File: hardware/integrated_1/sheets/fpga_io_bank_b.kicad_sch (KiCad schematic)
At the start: 1 part, among them U1 XC6SLX9-TQG144

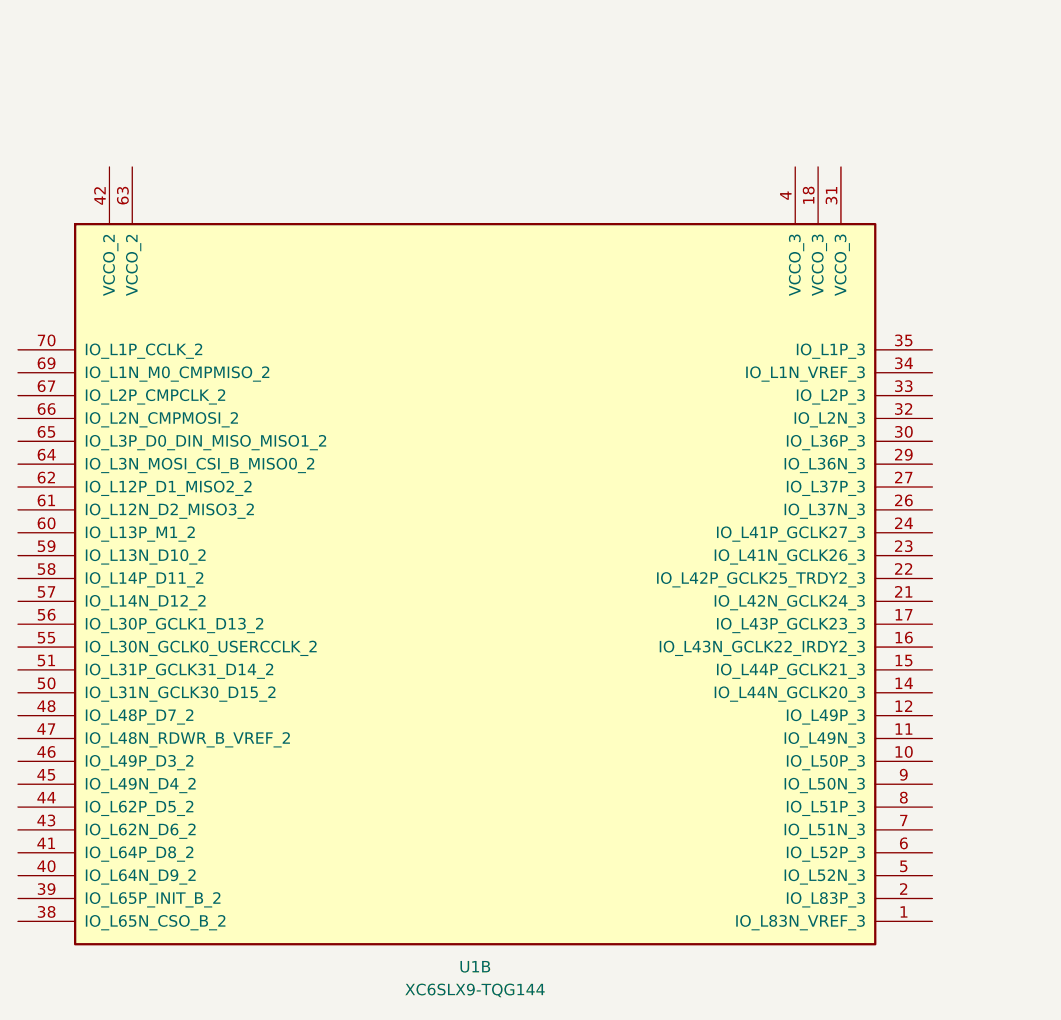
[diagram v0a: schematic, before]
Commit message: hooked up display to fpga
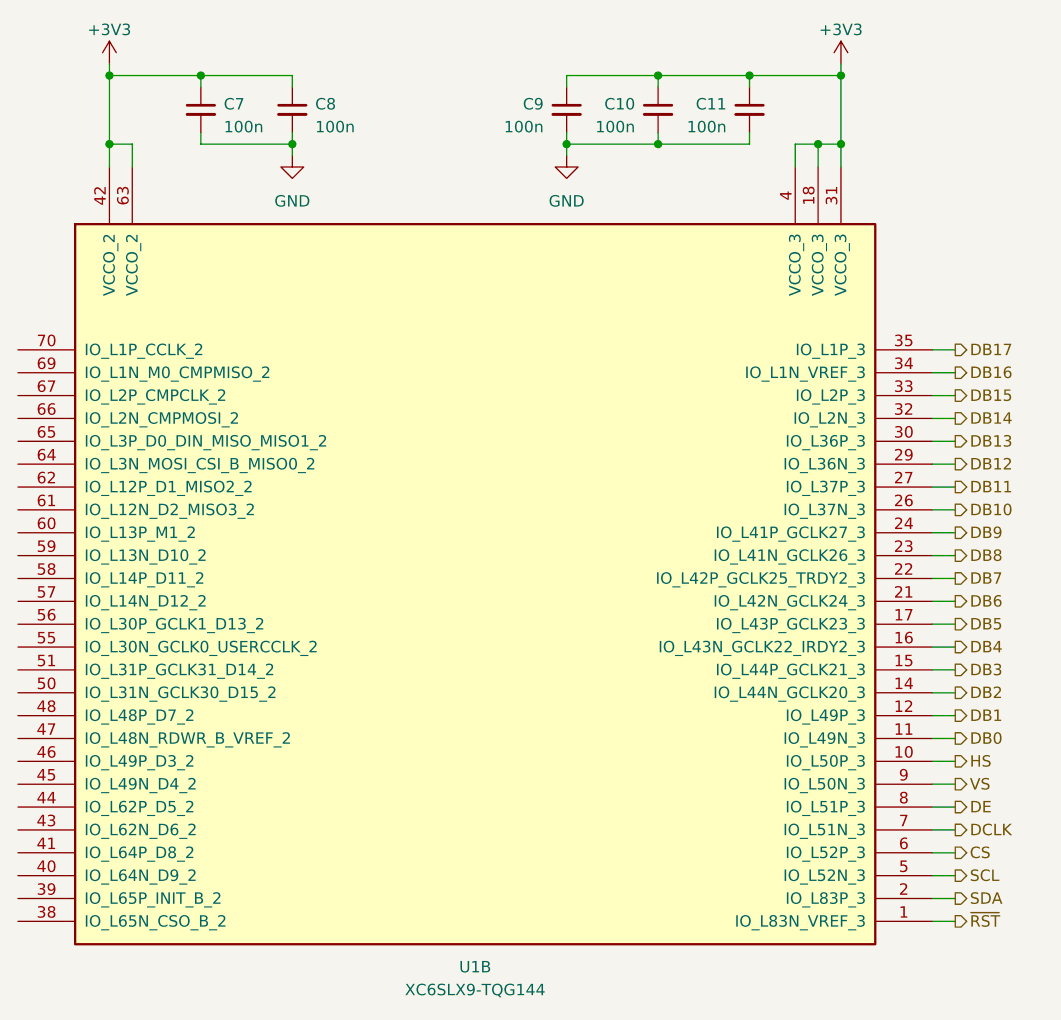
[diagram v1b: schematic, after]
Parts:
- added C10, C11, C7, C8, C9: 100n, Capacitor_SMD:C_0402_1005Metric, symbol Device:C_Small
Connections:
- net ~{RST}: now reaches U1.1 (IO_L83N_VREF_3)
- net HS: now reaches U1.10 (IO_L50P_3)
- net DB0: now reaches U1.11 (IO_L49N_3)
- net DB1: now reaches U1.12 (IO_L49P_3)
- net DB2: now reaches U1.14 (IO_L44N_GCLK20_3)
- net DB3: now reaches U1.15 (IO_L44P_GCLK21_3)
- net DB4: now reaches U1.16 (IO_L43N_GCLK22_IRDY2_3)
- net DB5: now reaches U1.17 (IO_L43P_GCLK23_3)
- net +3V3: now reaches U1.18 (VCCO_3)
- net +3V3: now also U1.31 (VCCO_3), U1.4 (VCCO_3), U1.42 (VCCO_2), U1.63 (VCCO_2), C10.1, C11.1, C7.1, C8.1, C9.1
- net SDA: now reaches U1.2 (IO_L83P_3)
- net DB6: now reaches U1.21 (IO_L42N_GCLK24_3)
- net DB7: now reaches U1.22 (IO_L42P_GCLK25_TRDY2_3)
- net DB8: now reaches U1.23 (IO_L41N_GCLK26_3)
- net DB9: now reaches U1.24 (IO_L41P_GCLK27_3)
- net DB10: now reaches U1.26 (IO_L37N_3)
- net DB11: now reaches U1.27 (IO_L37P_3)
- net DB12: now reaches U1.29 (IO_L36N_3)
- net DB13: now reaches U1.30 (IO_L36P_3)
- net DB14: now reaches U1.32 (IO_L2N_3)
- net DB15: now reaches U1.33 (IO_L2P_3)
- net DB16: now reaches U1.34 (IO_L1N_VREF_3)
- net DB17: now reaches U1.35 (IO_L1P_3)
- net SCL: now reaches U1.5 (IO_L52N_3)
- net CS: now reaches U1.6 (IO_L52P_3)
- net DCLK: now reaches U1.7 (IO_L51N_3)
- net DE: now reaches U1.8 (IO_L51P_3)
- net VS: now reaches U1.9 (IO_L50N_3)
- new net GND: C10.2, C11.2, C7.2, C8.2, C9.2

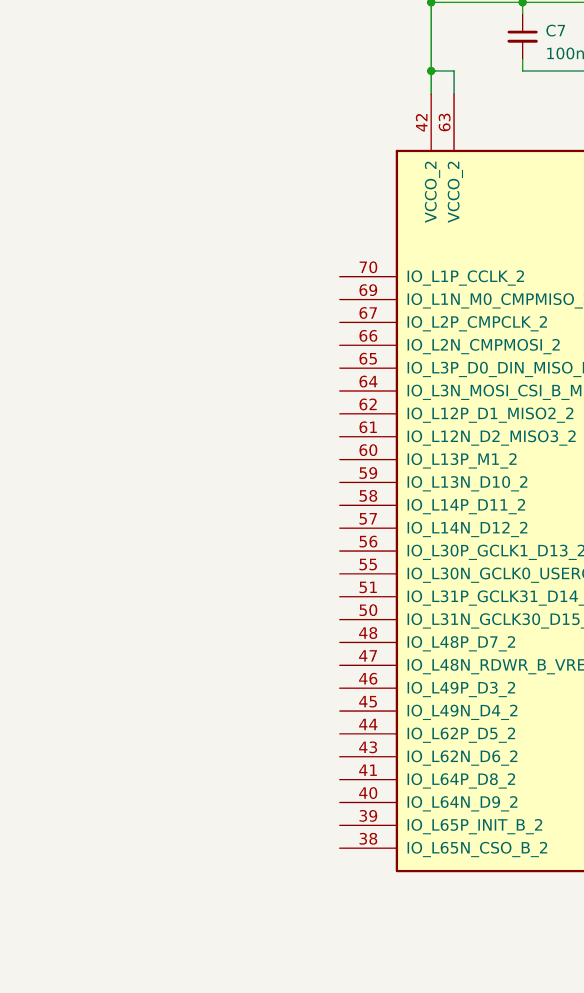
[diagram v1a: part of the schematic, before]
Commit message: rearranged the pinout to make more sense
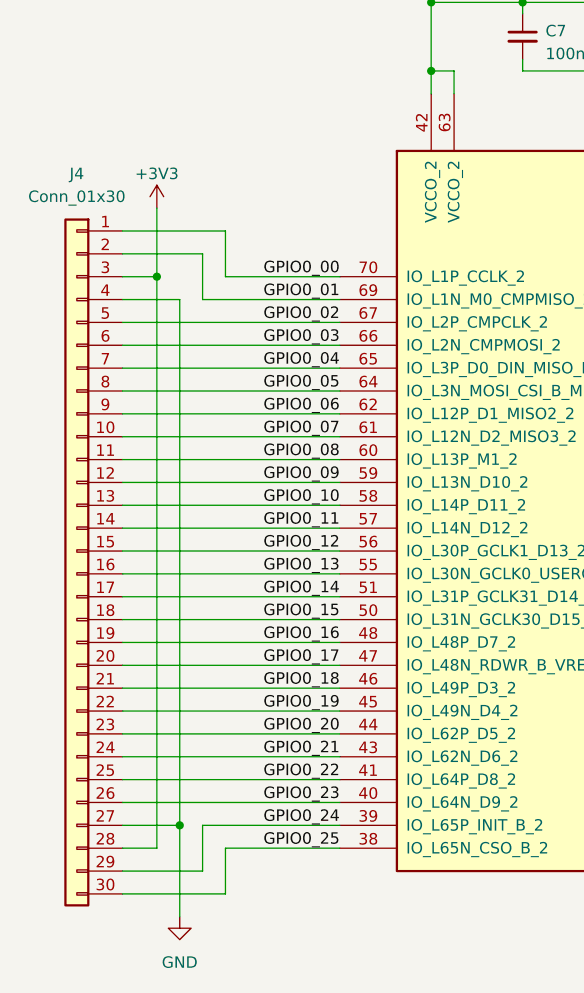
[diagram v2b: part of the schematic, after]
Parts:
- added J4: Conn_01x30, Connector_PinSocket_2.54mm:PinSocket_1x30_P2.54mm_Vertical, symbol Connector_Generic:Conn_01x30
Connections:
- net +3V3: now also J4.28 (Pin_28), J4.3 (Pin_3)
- net GND: now also J4.27 (Pin_27), J4.4 (Pin_4)
- net GPIO0_25: now reaches U1.38 (IO_L65N_CSO_B_2)
- net GPIO0_25: now also J4.30 (Pin_30)
- net GPIO0_24: now reaches U1.39 (IO_L65P_INIT_B_2)
- net GPIO0_24: now also J4.29 (Pin_29)
- net GPIO0_23: now reaches U1.40 (IO_L64N_D9_2)
- net GPIO0_23: now also J4.26 (Pin_26)
- net GPIO0_22: now reaches U1.41 (IO_L64P_D8_2)
- net GPIO0_22: now also J4.25 (Pin_25)
- net GPIO0_21: now reaches U1.43 (IO_L62N_D6_2)
- net GPIO0_21: now also J4.24 (Pin_24)
- net GPIO0_20: now reaches U1.44 (IO_L62P_D5_2)
- net GPIO0_20: now also J4.23 (Pin_23)
- net GPIO0_19: now reaches U1.45 (IO_L49N_D4_2)
- net GPIO0_19: now also J4.22 (Pin_22)
- net GPIO0_18: now reaches U1.46 (IO_L49P_D3_2)
- net GPIO0_18: now also J4.21 (Pin_21)
- net GPIO0_17: now reaches U1.47 (IO_L48N_RDWR_B_VREF_2)
- net GPIO0_17: now also J4.20 (Pin_20)
- net GPIO0_16: now reaches U1.48 (IO_L48P_D7_2)
- net GPIO0_16: now also J4.19 (Pin_19)
- net GPIO0_15: now reaches U1.50 (IO_L31N_GCLK30_D15_2)
- net GPIO0_15: now also J4.18 (Pin_18)
- net GPIO0_14: now reaches U1.51 (IO_L31P_GCLK31_D14_2)
- net GPIO0_14: now also J4.17 (Pin_17)
- net GPIO0_13: now reaches U1.55 (IO_L30N_GCLK0_USERCCLK_2)
- net GPIO0_13: now also J4.16 (Pin_16)
- net GPIO0_12: now reaches U1.56 (IO_L30P_GCLK1_D13_2)
- net GPIO0_12: now also J4.15 (Pin_15)
- net GPIO0_11: now reaches U1.57 (IO_L14N_D12_2)
- net GPIO0_11: now also J4.14 (Pin_14)
- net GPIO0_10: now reaches U1.58 (IO_L14P_D11_2)
- net GPIO0_10: now also J4.13 (Pin_13)
- net GPIO0_09: now reaches U1.59 (IO_L13N_D10_2)
- net GPIO0_09: now also J4.12 (Pin_12)
- net GPIO0_08: now reaches U1.60 (IO_L13P_M1_2)
- net GPIO0_08: now also J4.11 (Pin_11)
- net GPIO0_07: now reaches U1.61 (IO_L12N_D2_MISO3_2)
- net GPIO0_07: now also J4.10 (Pin_10)
- net GPIO0_06: now reaches U1.62 (IO_L12P_D1_MISO2_2)
- net GPIO0_06: now also J4.9 (Pin_9)
- net GPIO0_05: now reaches U1.64 (IO_L3N_MOSI_CSI_B_MISO0_2)
- net GPIO0_05: now also J4.8 (Pin_8)
- net GPIO0_04: now reaches U1.65 (IO_L3P_D0_DIN_MISO_MISO1_2)
- net GPIO0_04: now also J4.7 (Pin_7)
- net GPIO0_03: now reaches U1.66 (IO_L2N_CMPMOSI_2)
- net GPIO0_03: now also J4.6 (Pin_6)
- net GPIO0_02: now reaches U1.67 (IO_L2P_CMPCLK_2)
- net GPIO0_02: now also J4.5 (Pin_5)
- net GPIO0_01: now reaches U1.69 (IO_L1N_M0_CMPMISO_2)
- net GPIO0_01: now also J4.2 (Pin_2)
- net GPIO0_00: now reaches U1.70 (IO_L1P_CCLK_2)
- net GPIO0_00: now also J4.1 (Pin_1)

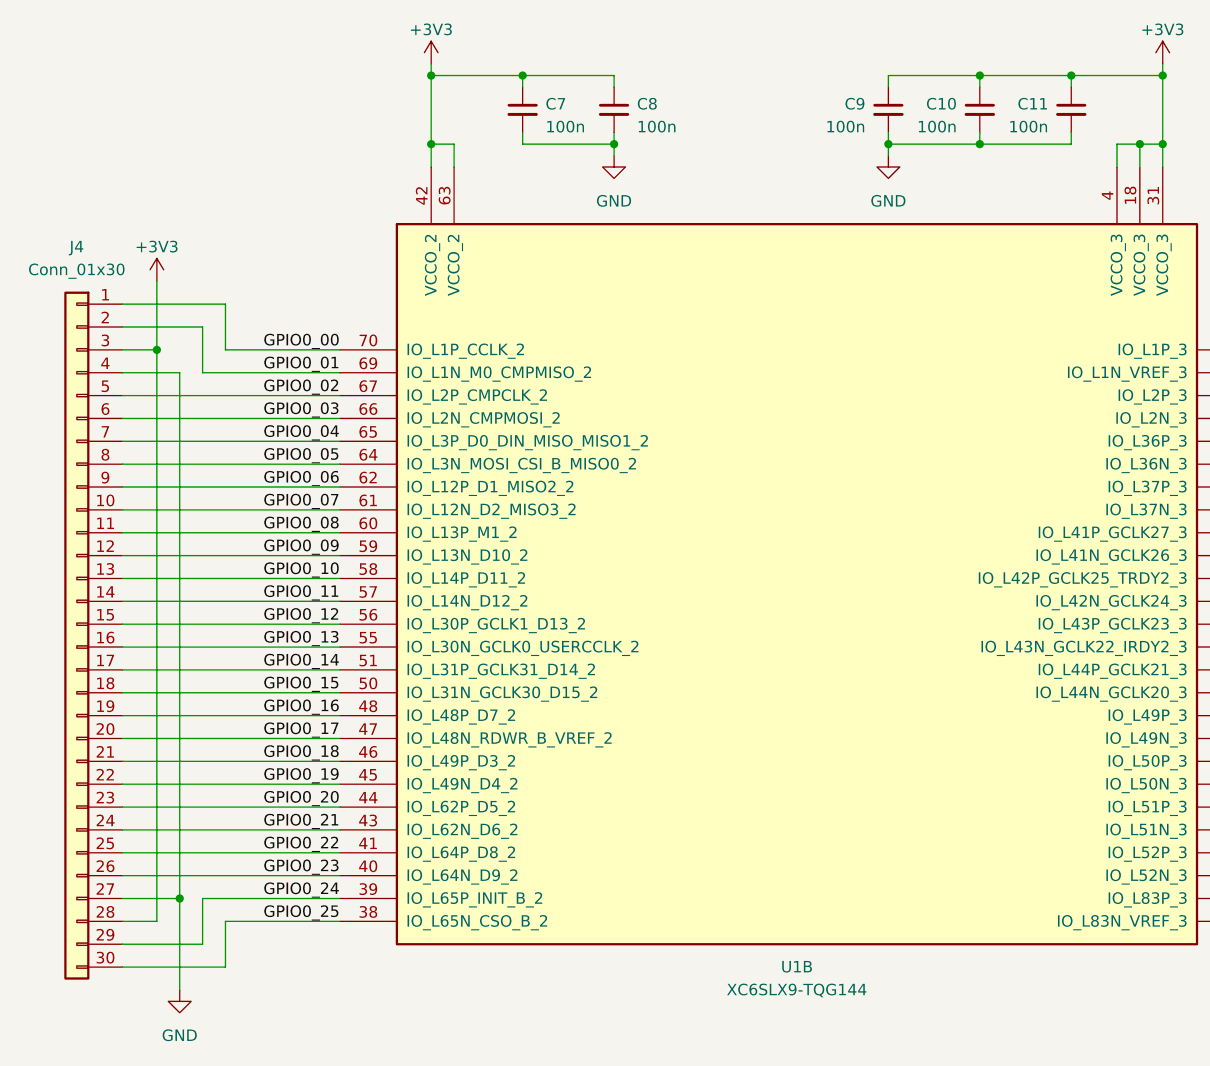
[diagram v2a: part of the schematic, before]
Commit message: reannotated schematic
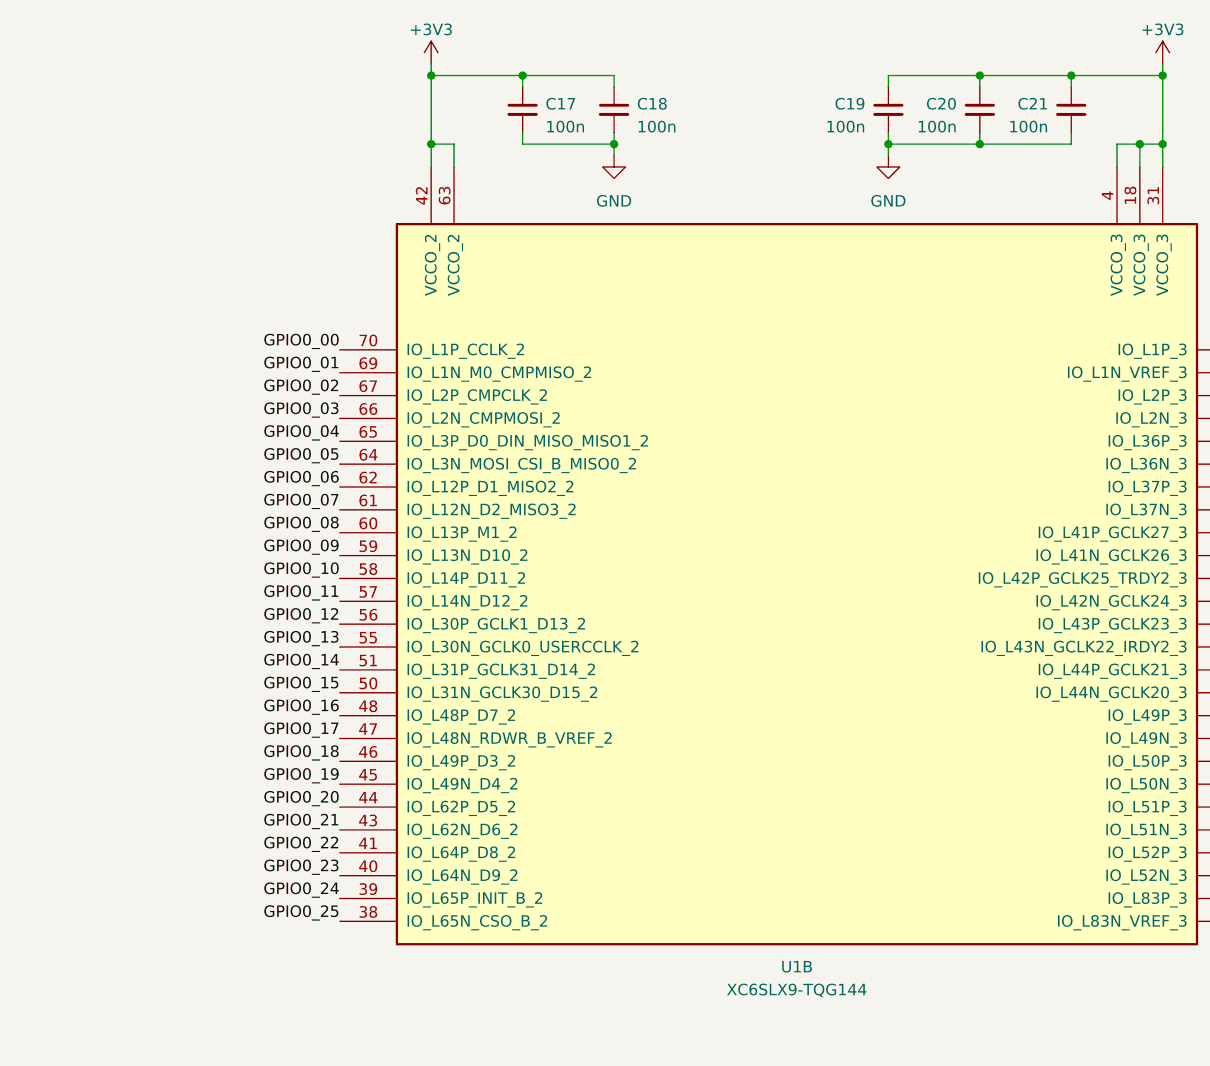
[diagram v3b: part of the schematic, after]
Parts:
- removed J4: Conn_01x30, Connector_PinSocket_2.54mm:PinSocket_1x30_P2.54mm_Vertical, symbol Connector_Generic:Conn_01x30
- C17: renamed from C7; footprint Capacitor_SMD:C_0402_1005Metric -> KiCAD Library:C_0402_1005Metric
- C18: renamed from C8; footprint Capacitor_SMD:C_0402_1005Metric -> KiCAD Library:C_0402_1005Metric
- C19: renamed from C9; footprint Capacitor_SMD:C_0402_1005Metric -> KiCAD Library:C_0402_1005Metric
- C20: renamed from C10; footprint Capacitor_SMD:C_0402_1005Metric -> KiCAD Library:C_0402_1005Metric
- C21: renamed from C11; footprint Capacitor_SMD:C_0402_1005Metric -> KiCAD Library:C_0402_1005Metric
